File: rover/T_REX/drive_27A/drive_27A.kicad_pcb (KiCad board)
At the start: 4 copper layers, 30 x 58.2 mm, 54 parts, among them J1 USB_B_Micro, J2 RJ45, J6 XT30PW-M, J7 XT30PW-F, J9 B4B-XH-A_LF__SN_, SW1 TS09-63-25-WT-160-SMT-TR, SW2 TS09-63-25-WT-160-SMT-TR, U2 TJA1050T_CM_118, U3 AZ1117ID-3.3TRG1, U4 BTN8962TA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

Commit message: .
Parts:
- removed H3: MountingHole_Pad, MountingHole:MountingHole_2.2mm_M2_DIN965_Pad_TopBottom
- added JP1: Jumper_3_Open, Connector_PinHeader_2.54mm:PinHeader_1x03_P2.54mm_Vertical, B.Cu at (45.0, 49.8)
- H1, H2: footprint MountingHole:MountingHole_2.2mm_M2_DIN965_Pad_TopBottom -> MountingHole:MountingHole_3.2mm_M3_DIN965_Pad_TopBottom
- U2: value TJA1050T_CM_118 -> SN65HVD232Q
- moved C8 6.25 mm to (43.5, 32.5)
- moved C6 5.32 mm to (44.8, 53.5)
- moved R11 3.95 mm to (27.0, 54.5)
- moved C12 2.40 mm to (42.5, 24.5)
- moved C11 2.20 mm to (18.5, 24.5)
- moved J1 1.25 mm to (45.2, 38.8)
- moved SW1 0.75 mm to (18.2, 26.5), turned to -90 degrees
- moved SW2 0.75 mm to (23.0, 26.5)
- moved H1 0.56 mm to (18.0, 18.2)
- moved H2 0.56 mm to (43.0, 18.2)
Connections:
- C3 pad 1: Net-(JP1-C) -> +3.3V
- C4 pad 1: Net-(JP1-C) -> +3.3V
- C5 pad 1: +5V -> Net-(JP1-C)
- J9 pad : GND -> (no net)
- U2 pad 3: Net-(JP1-C) -> +3.3V
- U3 pad 1: GND -> unconnected-(U3-GND-Pad1)
- U3 pad 2: +3.3V -> unconnected-(U3-OUTPUT-Pad2)
- U3 pad 3: +5V -> unconnected-(U3-INPUT-Pad3)
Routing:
- net EN_PB: track 42.3 -> 55.1 mm
- net J2-: track 1.65 -> 7.04 mm
- net GND: track 45.1 -> 49.4 mm, vias 40 -> 28
- net J2_EN_1: track 24.2 -> 26.0 mm, vias 1 -> 3
- net Net-(U4-IS): track 9.73 -> 11.4 mm
- net USB_N: track 15.9 -> 17.2 mm
- net USB_P: track 15.9 -> 17.2 mm
- net +5V: track 85.9 -> 87.2 mm
- net +24V: track 0.71 -> 0.00 mm
- net J2_IN_2: track 17.0 -> 17.7 mm
- net LED_BUILDIN: track 36.4 -> 37.0 mm
- net unconnected-(U3-OUTPUT-Pad2): vias 0 -> 20
- net +3.3V: vias 25 -> 5
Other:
- board size 30 x 58.2 mm -> 32.5 x 59.3 mm

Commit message: rev3 drive27A
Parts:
- removed the JP1 at (28.7, 71.8)
- U3: value AZ1117ID-3.3TRG1 -> LD1086DT33TR; footprint LDO_AZ1117ID-3.3TRG1:TO252-2_AZ1117ID-3.3TRG1_DIO -> LDO_AZ1117ID-3.3TRG1:TO252-2_AZ1117ID-3.3TRG1_DIO-L
- moved C16 5.45 mm to (34.2, 55.0)
- moved C6 4.84 mm to (43.0, 58.0), turned to 70 degrees
- moved C14 3.30 mm to (37.5, 50.6)
- moved R11 2.56 mm to (24.6, 55.4), turned to 90 degrees
- moved R12 1.57 mm to (37.5, 55.0), turned to 90 degrees
- moved J9 1.50 mm to (43.8, 27.5)
- moved C8 0.75 mm to (43.5, 31.8)
- moved R8 0.70 mm to (31.8, 50.6)
- turned C5 to -90 degrees
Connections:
- U3 pad 1: unconnected-(U3-GND-Pad1) -> GND
- U3 pad 2: unconnected-(U3-OUTPUT-Pad2) -> +3.3V
- U3 pad 3: unconnected-(U3-INPUT-Pad3) -> Net-(JP1-C)
- U6 pad 10: ENC_QUAD_A -> ENC_QUAD_B
- U6 pad 11: ENC_QUAD_B -> ENC_QUAD_A
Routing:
- net Net-(JP1-C): track 20.1 -> 46.5 mm, vias 0 -> 2
- net +3.3V: track 18.3 -> 35.5 mm, vias 5 -> 25
- net +5V: track 87.2 -> 79.9 mm, vias 4 -> 1
- net Net-(U5-SR): track 6.59 -> 13.1 mm
- net GND: track 49.4 -> 44.6 mm, vias 28 -> 27
- net ENC_QUAD_B: track 29.4 -> 25.4 mm
- net Net-(U4-IS): track 11.4 -> 14.1 mm
- net ENC_QUAD_A: track 22.2 -> 24.7 mm
- net Net-(U5-IS): track 12.5 -> 14.3 mm
- net USB_P: track 17.2 -> 16.3 mm
- net USB_N: track 17.2 -> 16.3 mm
- net Net-(U5-IN): track 8.18 -> 7.41 mm
- net J2-: track 7.04 -> 7.60 mm
- net J2_EN_1: track 26.0 -> 26.5 mm
- net unconnected-(U3-OUTPUT-Pad2): vias 20 -> 0
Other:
- board text added: "*"
- board text added: "Prog"
- board text removed: "3.3V"
- board text removed: "5V"

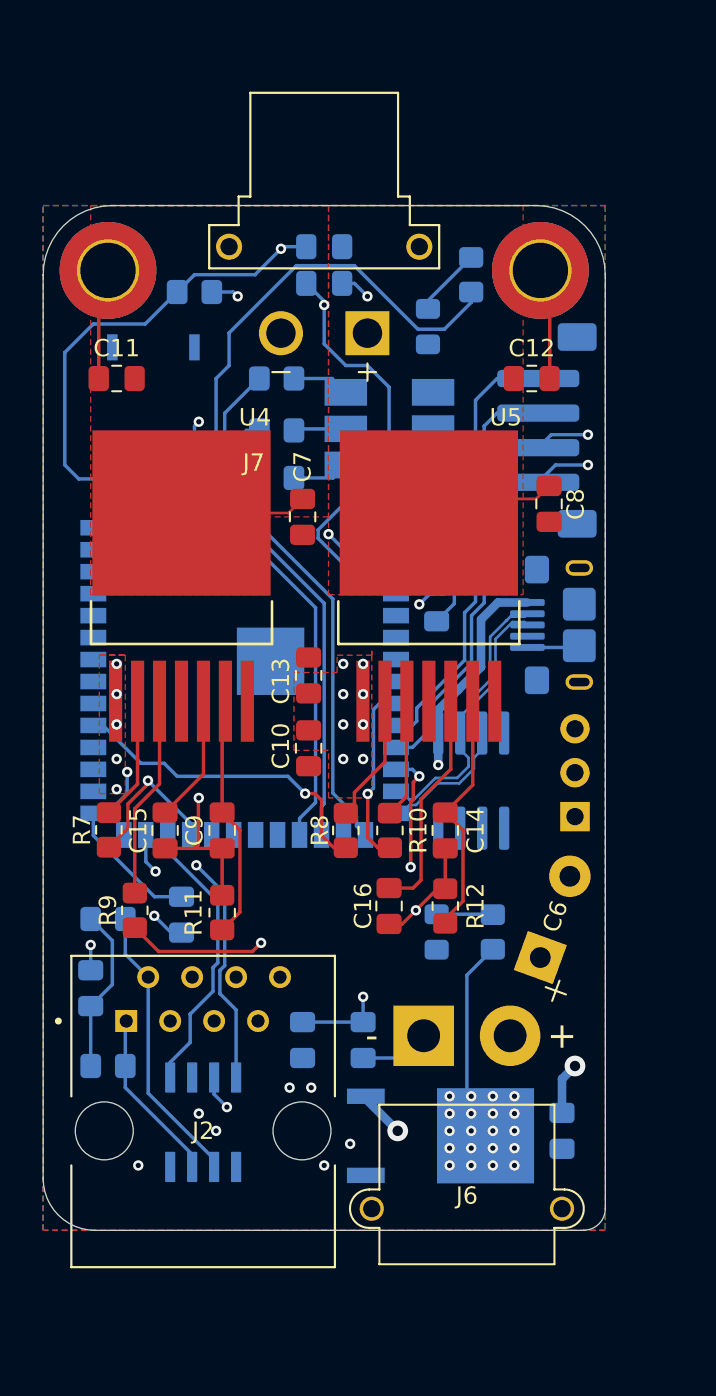
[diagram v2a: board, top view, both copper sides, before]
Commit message: edge cut adjustement
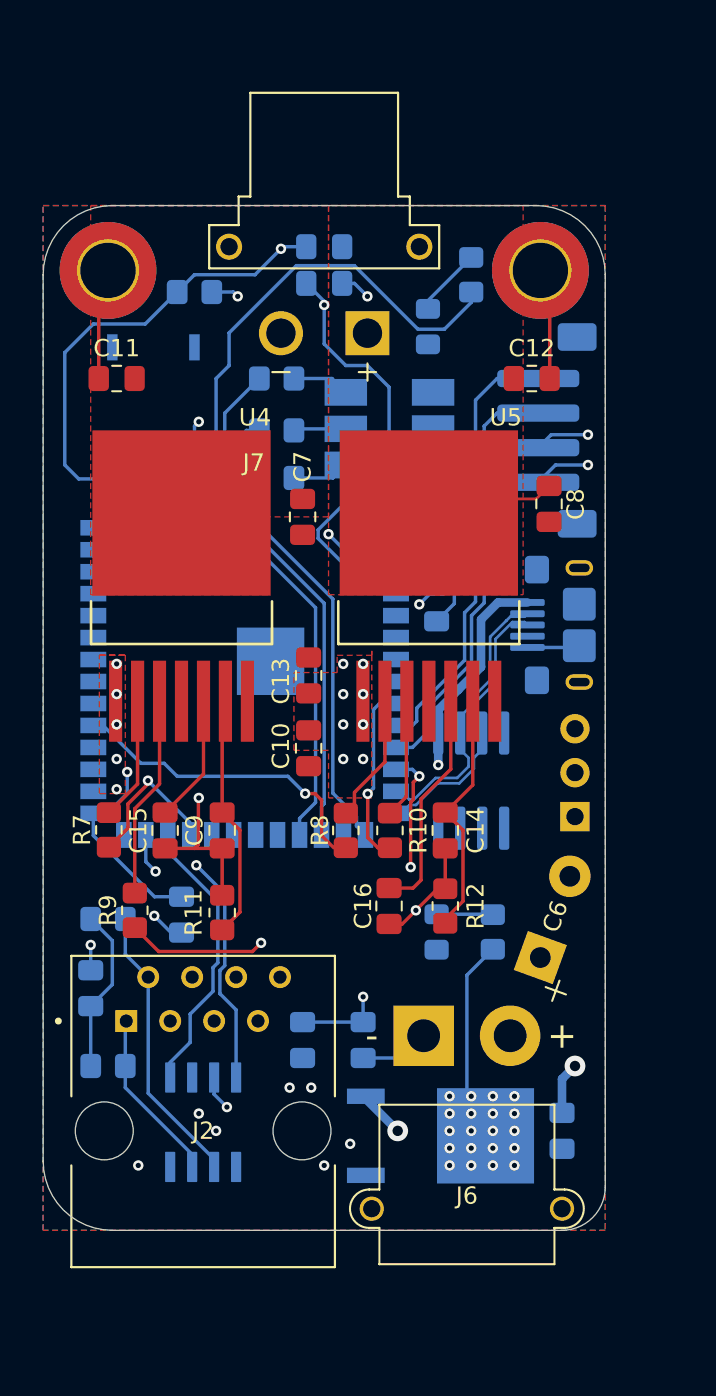
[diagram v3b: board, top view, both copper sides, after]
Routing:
- net J2+: track 11.9 -> 4.60 mm
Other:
- outline, holes or cut-outs redrawn
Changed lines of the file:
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@@
 	)
 	(gr_arc
-		(start 46.754998 72.5)
-		(mid 46.383897 73.380939)
-		(end 45.5 73.744938)
+		(start 18.25 73.75)
+		(mid 15.421573 72.578427)
+		(end 14.25 69.75)
+		(stroke
+			(width 0.05)
+			(type default)
+		)
+		(layer "Edge.Cuts")
+	)
+	(gr_arc
+		(start 46.75 71.25)
+		(mid 46.017767 73.017767)
+		(end 44.25 73.75)
 		(stroke
 			(width 0.05)
@@
 		(layer "Edge.Cuts")
 	)
-	(gr_arc
-		(start 17.25 73.75)
-		(mid 15.12868 72.87132)
-		(end 14.25 70.75)
-		(stroke
-			(width 0.05)
-			(type default)
-		)
-		(layer "Edge.Cuts")
-	)
 	(gr_line
 		(start 18.25 14.5)
@@
 	)
 	(gr_line
-		(start 17.25 73.75)
-		(end 45.5 73.75)
+		(start 18.25 73.75)
+		(end 44.25 73.75)
 		(stroke
 			(width 0.05)
@@
 	(gr_line
 		(start 14.25 18.5)
-		(end 14.25 70.75)
+		(end 14.25 69.75)
 		(stroke
 			(width 0.05)
@@
 	)
 	(gr_line
-		(start 46.754999 72.5)
+		(start 46.75 71.25)
 		(end 46.75 18.499999)
 		(stroke
@@
 		(width 0.155814)
 		(layer "F.Cu")
-		(net 6)
-	)
-	(segment
-		(start 28.4338 32.2787)
-		(end 29.25 31.4625)
-		(width 0.155814)
-		(layer "F.Cu")
-		(net 6)
-	)
-	(segment
-		(start 22.25 32.2787)
-		(end 28.4338 32.2787)
-		(width 0.155814)
-		(layer "F.Cu")

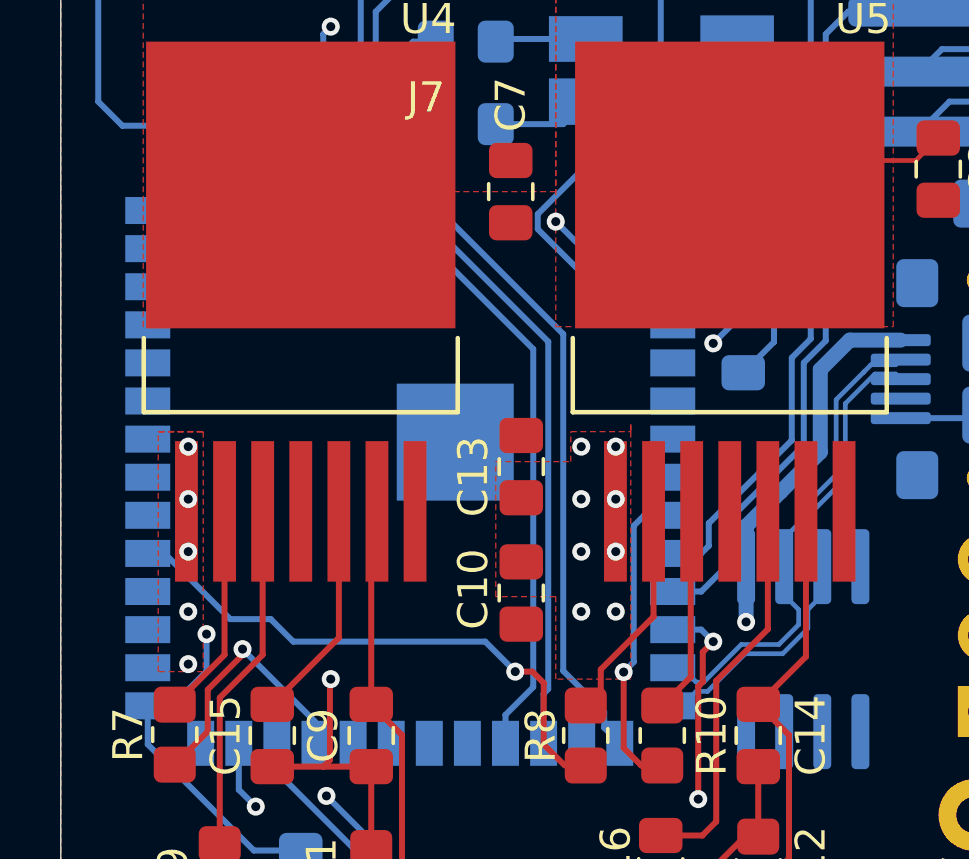
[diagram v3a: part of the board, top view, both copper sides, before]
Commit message: Drive27A Thermal design validation
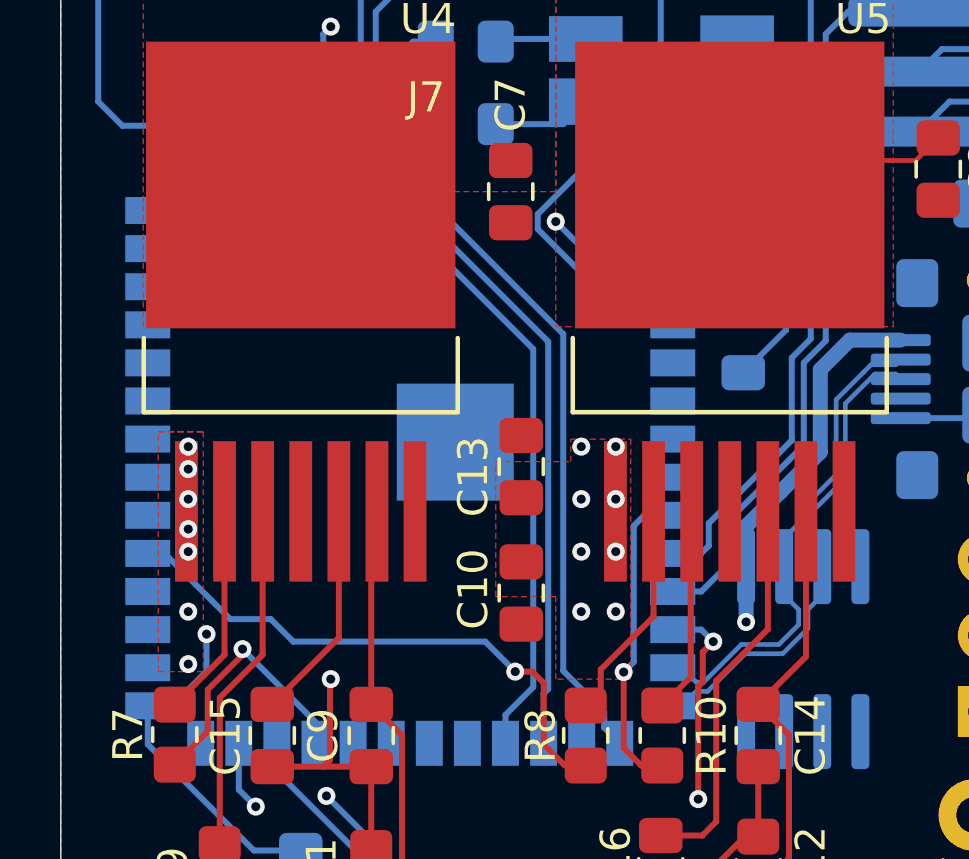
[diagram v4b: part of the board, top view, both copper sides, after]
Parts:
- turned C17 to -90 degrees
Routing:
- net GND: track 44.6 -> 50.6 mm, vias 27 -> 28
- net +3.3V: track 35.5 -> 33.6 mm

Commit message: new drive 27A
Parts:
- J6: value XT30PW-M -> XT60PW-M; footprint Connector_AMASS:AMASS_XT30PW-M_1x02_P2.50mm_Horizontal -> Connector_AMASS:AMASS_XT60PW-M_1x02_P7.20mm_Horizontal
- J7: value XT30PW-F -> XT60PW-F; footprint XT30PW-F:AMASS_XT30PW-F -> Connector_AMASS:AMASS_XT60PW-F_1x02_P7.20mm_Horizontal
- moved J7 6.38 mm to (34.1, 22.1)
- moved J6 6.11 mm to (42.4, 62.8)
- moved D1 4.93 mm to (34.0, 17.2)
- moved R14 3.72 mm to (30.5, 22.0), turned to 90 degrees
- moved J2 3.55 mm to (22.3, 71.3)
- moved C19 2.77 mm to (27.8, 17.2), turned to 90 degrees
- moved U2 2.36 mm to (22.2, 69.5), turned to 180 degrees
- moved R1 2.26 mm to (38.8, 20.8)
- moved R3 2.25 mm to (15.8, 64.2), turned to -90 degrees
- moved C1 1.75 mm to (30.5, 17.2), turned to -90 degrees
- moved C3 1.06 mm to (32.0, 63.5), turned to 90 degrees
- moved C4 1.06 mm to (28.5, 63.5), turned to 90 degrees
- moved U3 0.88 mm to (37.2, 68.8)
- moved C5 0.75 mm to (43.5, 68.0)
- moved D2 0.75 mm to (36.2, 56.5)
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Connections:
- J6 pad 1: GND -> +24V
- J6 pad 2: +24V -> GND
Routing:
- net TXC: track 18.3 -> 27.8 mm, vias 2 -> 4
- net LED_BUILDIN: track 37.0 -> 30.6 mm, vias 0 -> 2
- net GND: track 50.6 -> 56.8 mm, vias 28 -> 39
- net LED_B: track 29.8 -> 35.8 mm
- net RXC: track 16.4 -> 21.0 mm
- net +5V: track 79.9 -> 76.3 mm
- net +3.3V: track 33.6 -> 37.1 mm, vias 25 -> 23
- net EN_PB: track 55.3 -> 52.2 mm
- net CANH: track 10.1 -> 7.35 mm
- net Net-(D1-A): track 4.01 -> 6.21 mm
- net CANL: track 16.5 -> 17.9 mm
- net Net-(JP1-C): track 46.5 -> 45.5 mm
- net Net-(D3-Pad3): track 3.33 -> 2.82 mm

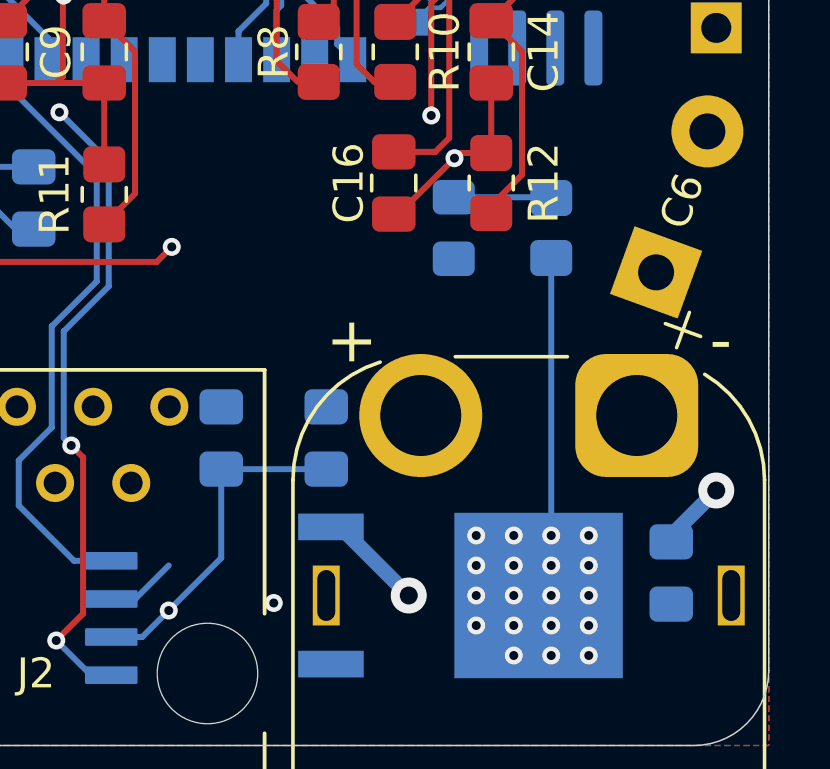
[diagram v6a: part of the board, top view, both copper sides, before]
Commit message: Edit switched power pins
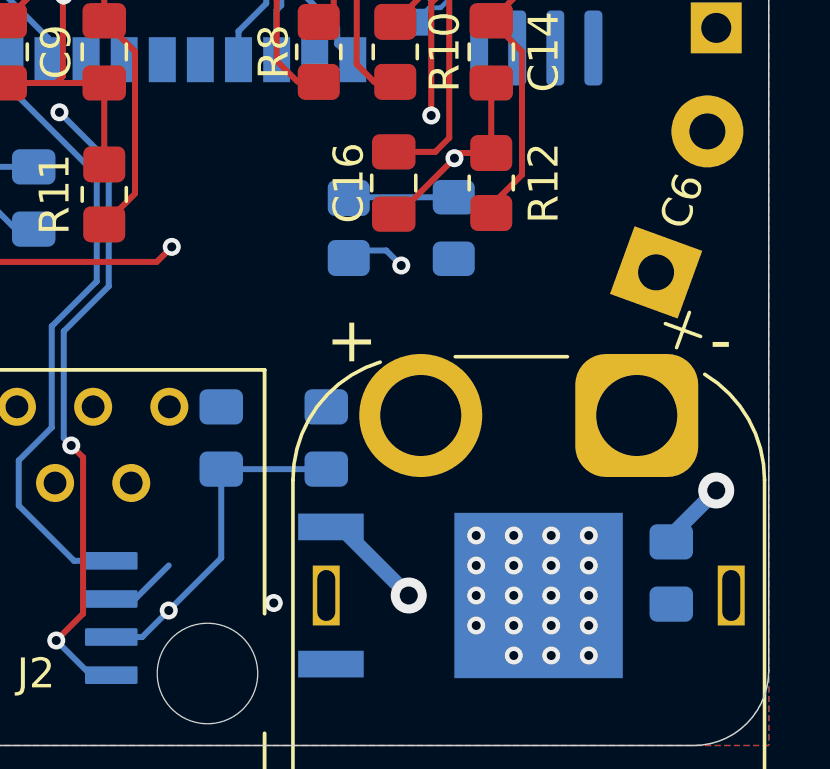
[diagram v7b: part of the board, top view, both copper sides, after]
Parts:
- moved R2 6.75 mm to (32.8, 56.5)
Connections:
- J6 pad 1: +24V -> GND
- J6 pad 2: GND -> +24V
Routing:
- net +3.3V: track 37.1 -> 28.6 mm, vias 23 -> 24
- net GND: track 56.8 -> 53.1 mm
- net +24V: track 0.00 -> 3.64 mm
